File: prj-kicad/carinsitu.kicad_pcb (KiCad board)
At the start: 2 copper layers, 120 x 50 mm, 67 parts, among them P1 BAT, P2 MOT, P3 CONN_3, P4 CONN_4, SW1 SWITCH_SLIDE, SW2 Reset, U1 LoLin_D1_mini_pro, U2 MIC2860, U3 MAX17044G, U4 SN74LV1T34DBV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

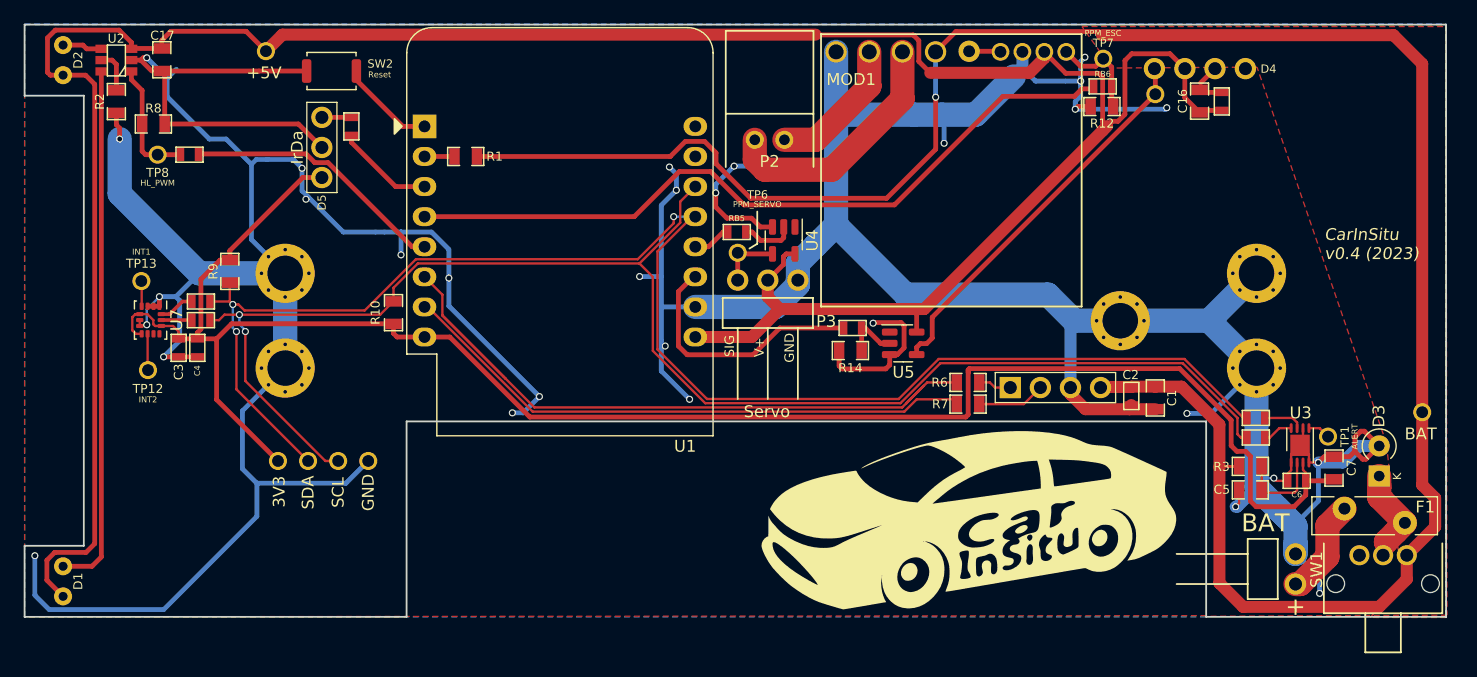
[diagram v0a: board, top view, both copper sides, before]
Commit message: Change some footprints for kicad lib ones + silkscreen + route adjustments
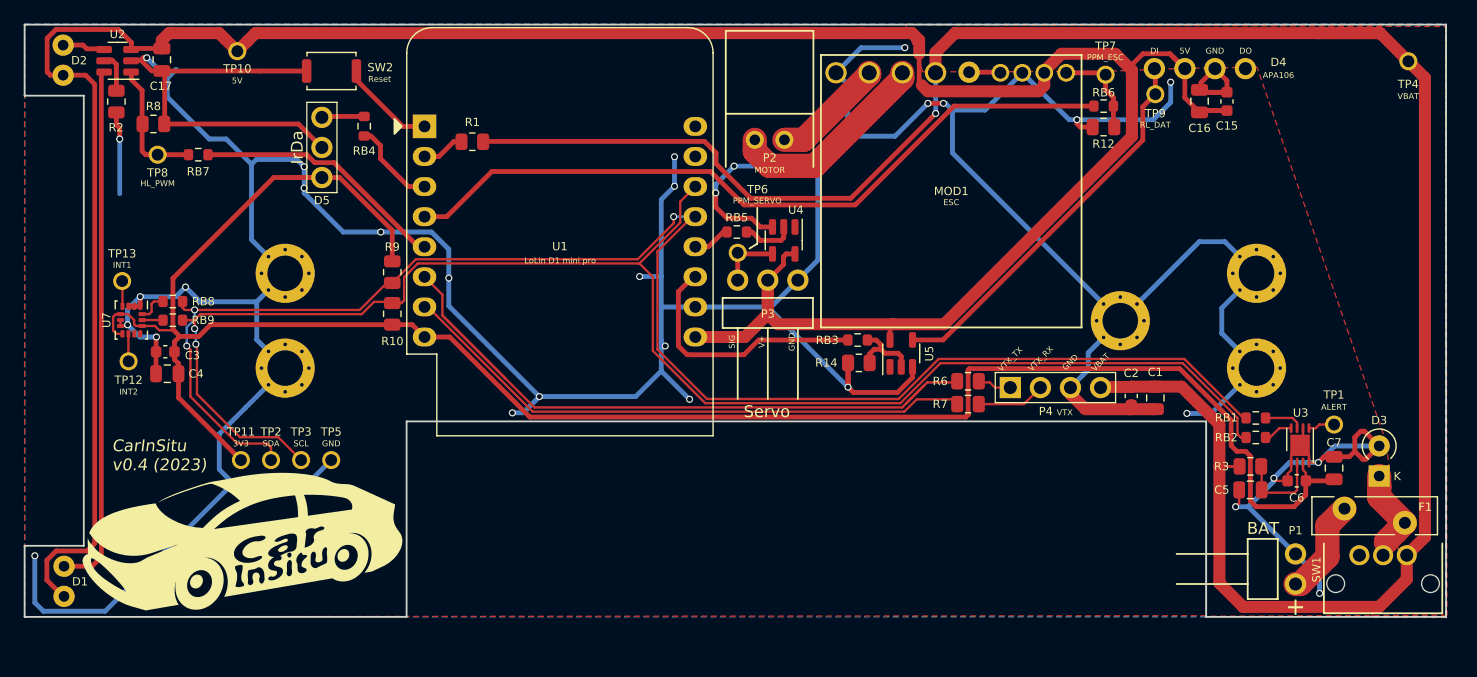
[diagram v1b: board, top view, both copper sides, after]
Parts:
- removed the G*** at (162.5, 121.8)
- added G***: LOGO, logo_carinsitu, F.Cu at (101.1, 123.6)
- C1, C16, C17, C5, C7: footprint carinsitu:SMD0805 -> Capacitor_SMD:C_0805_2012Metric
- C15, C2, C3, C6: footprint carinsitu:SMD0603 -> Capacitor_SMD:C_0603_1608Metric
- C4: footprint carinsitu:SMD0603 -> Capacitor_SMD:C_0805_2012Metric
- D1, D2: footprint carinsitu:LED -> LED_THT:LED_D5.0mm_Horizontal_O3.81mm_Z3.0mm; moved to B.Cu
- R1, R10, R12, R14, R2, R3, R6, R7, R8, R9: footprint carinsitu:SMD0805 -> Resistor_SMD:R_0805_2012Metric
- RB1, RB2, RB3, RB4, RB5, RB6, RB7, RB8, RB9: footprint carinsitu:SMD0603 -> Resistor_SMD:R_0603_1608Metric
- U2: footprint carinsitu:SOT23-6 -> Package_TO_SOT_SMD:SOT-23-6
- moved TP4 29.6 mm to (199.6, 83.1)
- moved R9 13.7 mm to (113.8, 100.9)
- moved C4 3.35 mm to (94.8, 109.5), turned to 0 degrees
- moved TP11 3.13 mm to (101.0, 116.8)
- moved TP2 3.13 mm to (103.6, 116.8)
- moved TP3 3.13 mm to (106.1, 116.8)
- moved TP5 3.13 mm to (108.6, 116.8)
- moved TP10 2.41 mm to (100.7, 82.2)
- moved RB8 2.38 mm to (95.3, 103.4)
- moved RB9 2.38 mm to (95.3, 105.0)
- moved TP12 1.80 mm to (91.5, 108.4)
- moved MOD1 1.77 mm to (161.0, 94.1)
- moved R12 1.74 mm to (173.8, 88.7)
- moved RB6 1.67 mm to (173.8, 86.9)
- moved TP13 1.62 mm to (91.0, 101.7)
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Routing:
- net GND: track 474.7 -> 440.9 mm, vias 30 -> 31
- net +3V3: track 156.9 -> 171.8 mm
- net +5V: track 228.0 -> 238.6 mm
- net Net-(MOD1-Pad3): track 21.0 -> 17.4 mm
- net SCL: track 128.4 -> 131.6 mm
- net Net-(MOD1-Pad2): track 12.0 -> 9.58 mm
- net RL_DAT: track 4.81 -> 6.42 mm
- net SDA: track 129.8 -> 131.3 mm
- net Net-(RB7-Pad1): track 22.3 -> 21.0 mm
- net Net-(R1-Pad1): track 2.52 -> 3.64 mm
- net IR_RX: track 2.49 -> 3.49 mm
- net +VBAT: track 185.2 -> 186.1 mm
- net Net-(RB9-Pad2): track 2.57 -> 1.75 mm
- net Net-(RB4-Pad1): track 8.31 -> 7.51 mm
- net Net-(TP12-Pad1): track 3.03 -> 2.31 mm
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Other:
- board text removed: "+5V"
- board text removed: "3V3"
- board text removed: "BAT"
- board text removed: "GND"
- board text removed: "SCL"
- board text removed: "SDA"

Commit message: Add decoupling capacitors + RB10
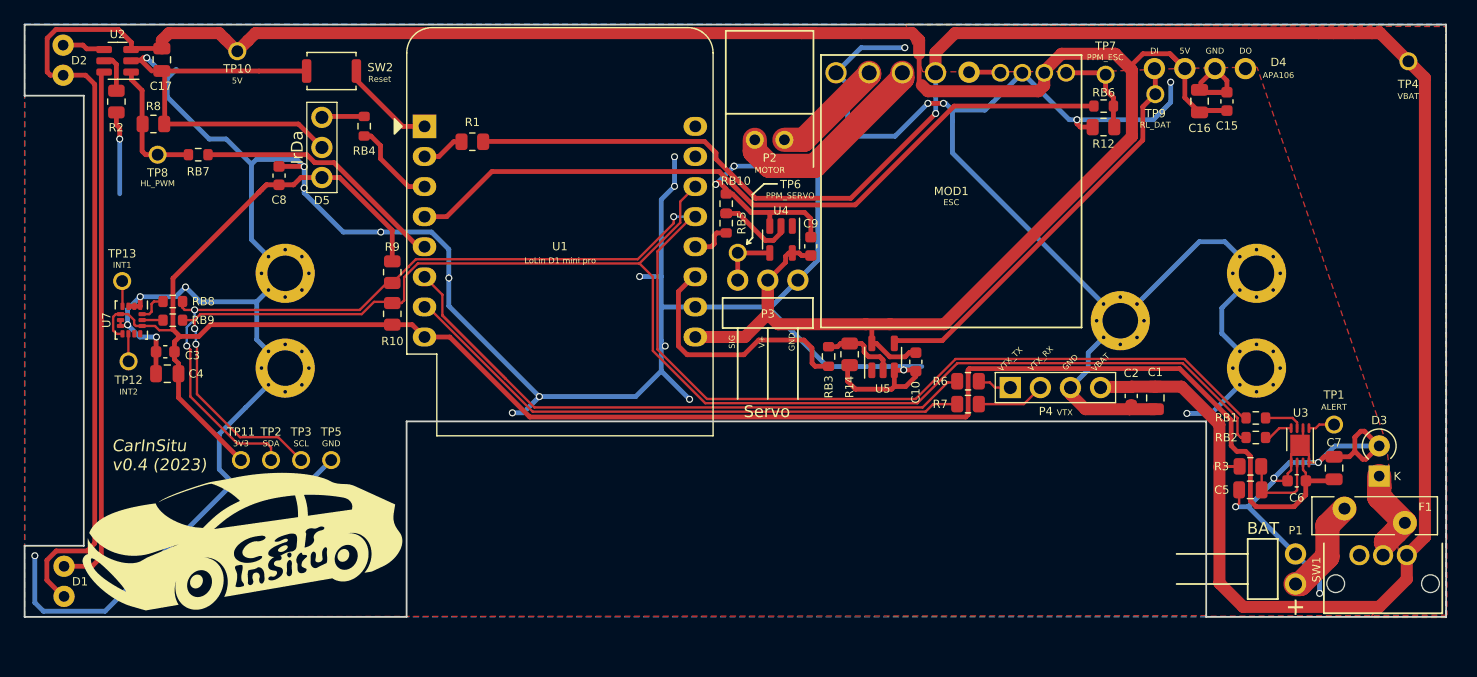
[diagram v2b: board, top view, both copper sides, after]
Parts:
- added C10: 100nF, Capacitor_SMD:C_0603_1608Metric, F.Cu at (158.0, 108.5)
- added C8: 100nF, Capacitor_SMD:C_0603_1608Metric, F.Cu at (104.2, 92.8)
- added C9: 100nF, Capacitor_SMD:C_0603_1608Metric, F.Cu at (149.1, 98.7)
- added RB10: DNP, Resistor_SMD:R_0603_1608Metric, F.Cu at (142.0, 95.1)
- moved RB3 2.82 mm to (150.6, 108.0), turned to 90 degrees
- moved U5 1.56 mm to (155.2, 108.1)
- moved RB5 1.16 mm to (142.0, 96.8), turned to 90 degrees
- moved R14 1.06 mm to (152.4, 107.8), turned to 90 degrees
- moved U4 0.24 mm to (146.6, 98.1)
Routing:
- net GND: track 440.9 -> 453.9 mm
- net +5V: track 238.6 -> 244.5 mm
- net /LOLIN_RX_SWAP: track 61.1 -> 58.9 mm
- net PPM_SERVO: track 4.50 -> 6.41 mm
- net Net-(D4-Pad4): track 32.8 -> 34.5 mm
- net +3V3: track 171.8 -> 170.4 mm

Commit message: Move U3 and its companions
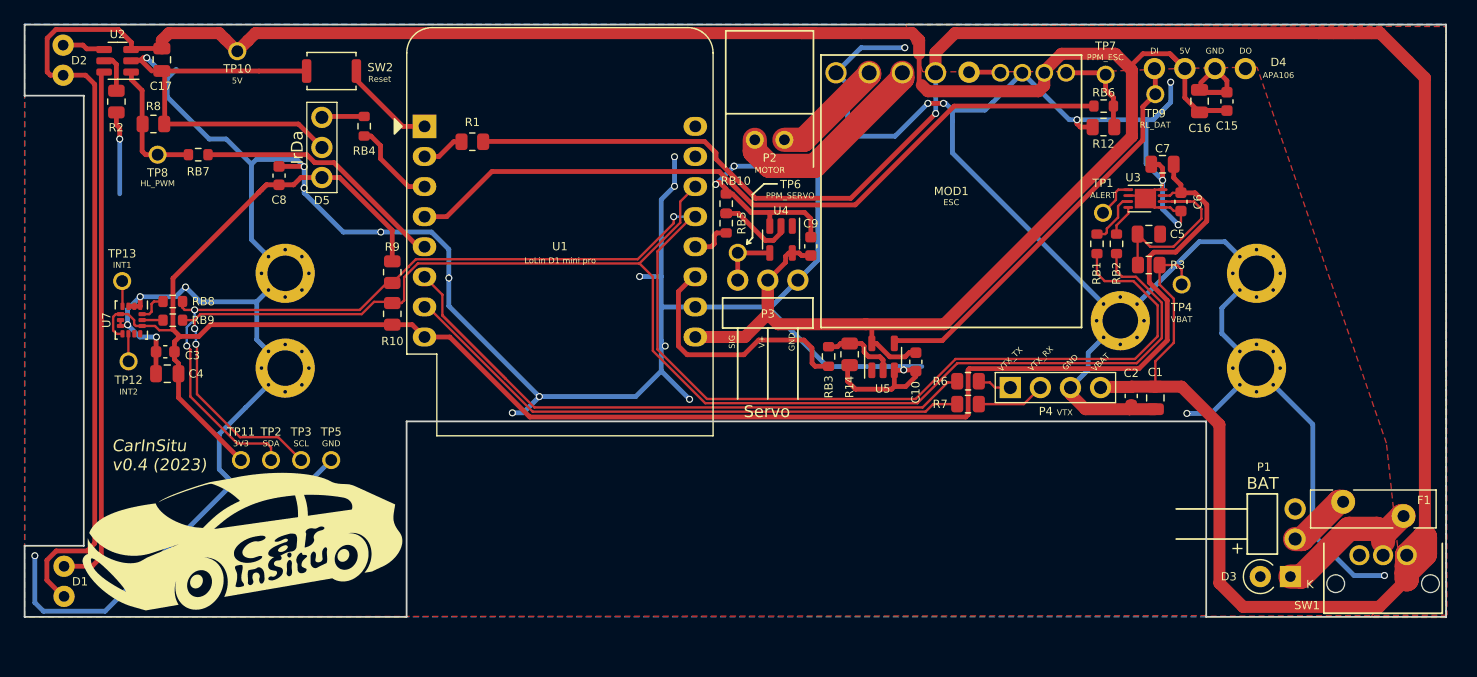
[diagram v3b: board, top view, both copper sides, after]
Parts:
- moved C7 29.5 mm to (178.8, 91.8), turned to 180 degrees
- moved TP4 26.9 mm to (180.4, 101.9)
- moved TP1 26.5 mm to (173.8, 95.9)
- moved C6 25.5 mm to (180.4, 95.0), turned to -90 degrees
- moved U3 24.6 mm to (177.4, 94.7), turned to 180 degrees
- moved C5 23.2 mm to (177.7, 97.7), turned to 0 degrees
- moved RB2 20.1 mm to (174.9, 98.5), turned to -90 degrees
- moved RB1 19.9 mm to (173.3, 98.5), turned to -90 degrees
- moved R3 19.0 mm to (177.7, 100.3), turned to 180 degrees
- moved D3 11.3 mm to (189.6, 126.6), turned to 180 degrees
- moved P1 3.80 mm to (190.0, 122.2)
- moved F1 0.58 mm to (199.2, 121.5)
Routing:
- net +VBAT: track 185.8 -> 205.3 mm
- net Net-(C5-Pad1): track 7.15 -> 15.3 mm
- net Net-(D3-Pad1): track 9.56 -> 13.8 mm
- net Net-(F1-Pad2): track 8.31 -> 5.35 mm
- net +3V3: track 170.4 -> 167.9 mm
- net GND: track 453.9 -> 451.5 mm, vias 31 -> 30
- net SDA: track 131.3 -> 133.3 mm
- net Net-(RB1-Pad1): track 3.36 -> 4.53 mm
- net Net-(TP1-Pad1): track 2.25 -> 3.33 mm
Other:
- board text removed: "+"

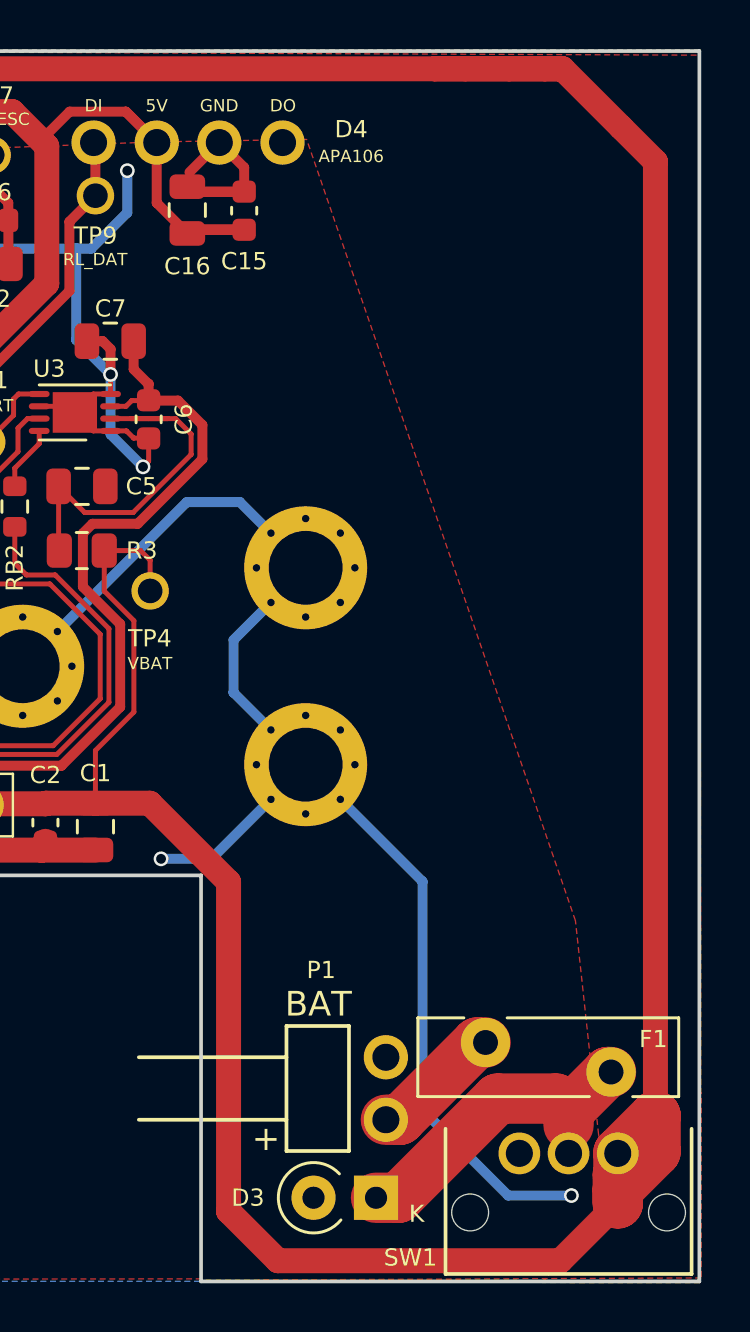
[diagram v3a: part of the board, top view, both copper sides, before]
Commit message: Add VTX holes (WIP, bottom right needs rerouting)
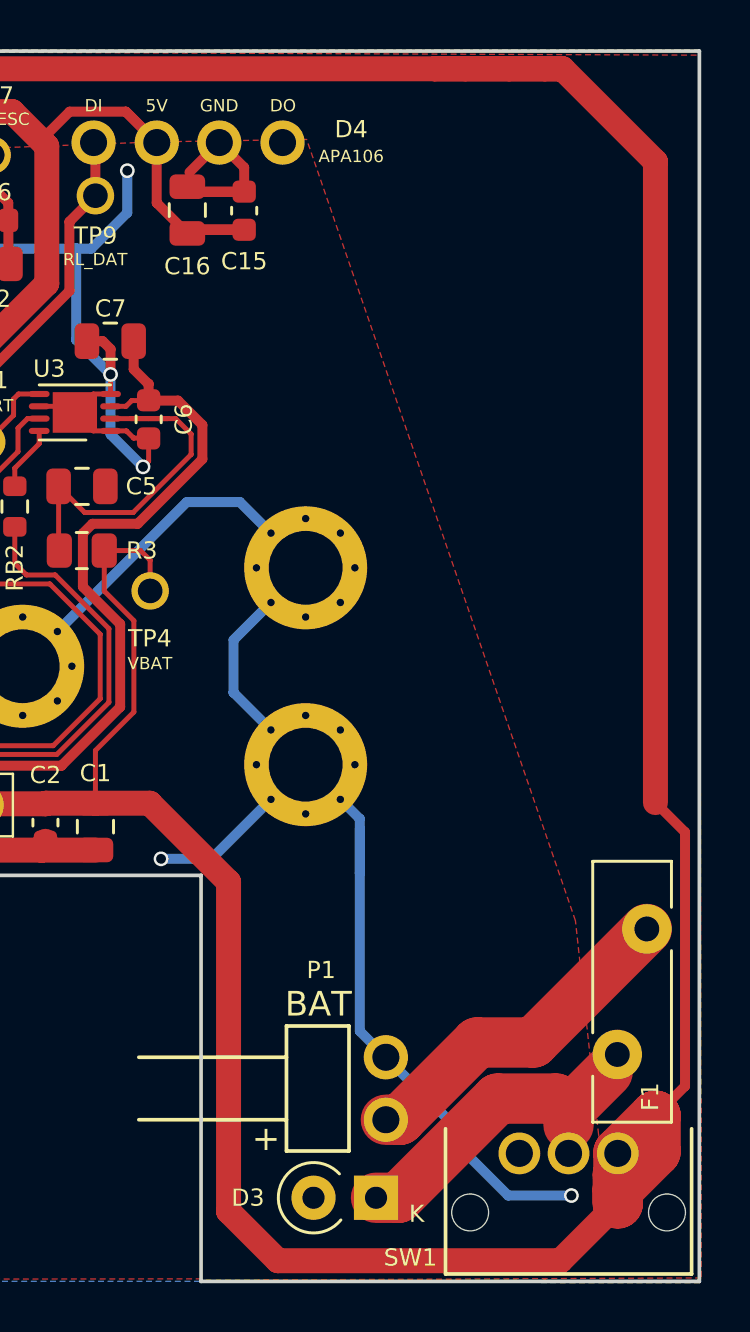
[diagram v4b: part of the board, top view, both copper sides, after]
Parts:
- added H1: VTX_avatar_halfholes, carinsitu:VTX_avatar_halfholes, F.Cu at (181.0, 105.0)
- moved F1 0.76 mm to (199.4, 120.8), turned to 90 degrees
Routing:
- net Net-(F1-Pad2): track 5.35 -> 13.8 mm
- net GND: track 451.5 -> 453.4 mm

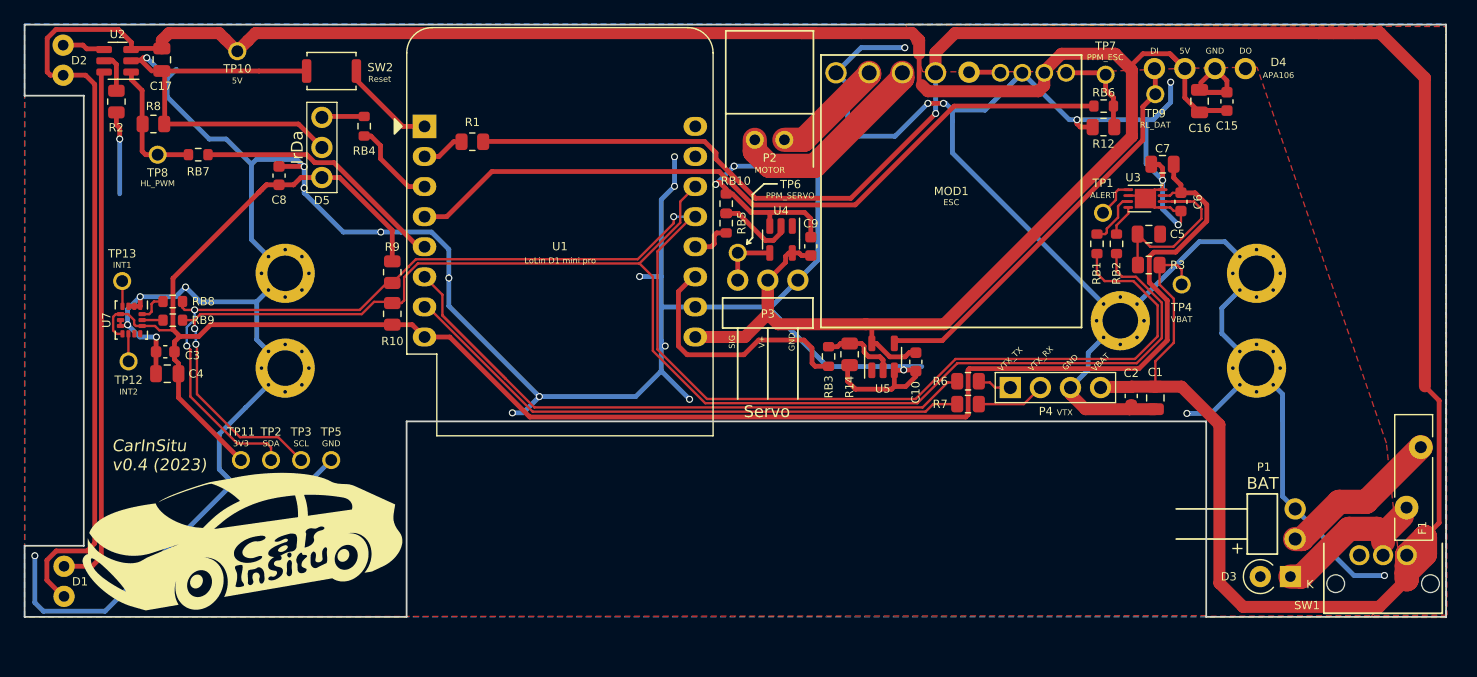
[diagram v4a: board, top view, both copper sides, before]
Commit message: Change input protection and its routing
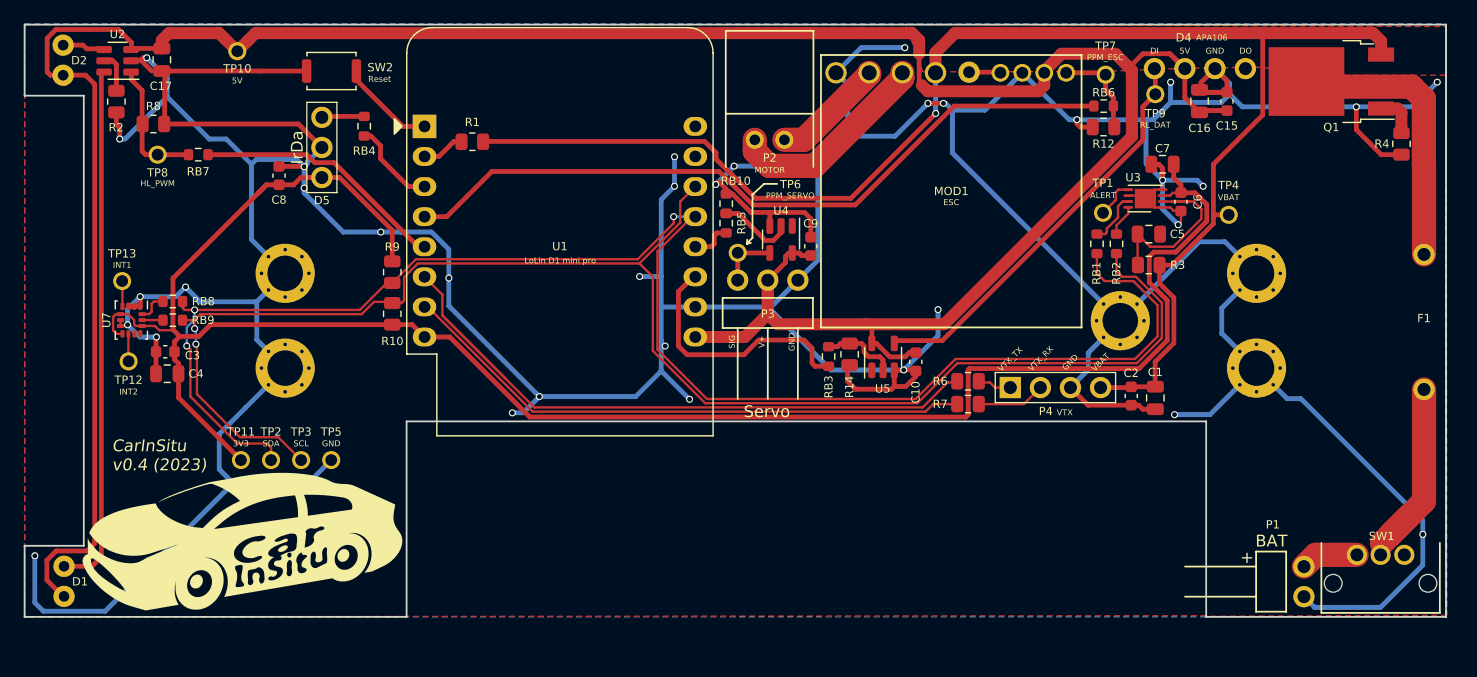
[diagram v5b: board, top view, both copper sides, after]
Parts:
- removed D3: D, Diode_THT:D_A-405_P2.54mm_Vertical_KathodeUp
- added Q1: TJ15P04M3, Package_TO_SOT_SMD:TO-252-2, F.Cu at (193.1, 84.8)
- added R4: 1k, Resistor_SMD:R_0805_2012Metric, F.Cu at (199.0, 90.1)
- F1: value Polyfuse -> Fuse_Small; footprint Fuse:Fuse_Bourns_MF-RG500 -> Fuse:Fuse_Littelfuse-LVR100
- H1: value VTX_avatar_halfholes -> MountingHole
- moved F1 10.1 mm to (200.9, 110.8)
- moved TP4 7.09 mm to (184.4, 96.1)
- moved P1 4.92 mm to (190.8, 127.0)
- moved SW1 0.21 mm to (195.2, 124.8)
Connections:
- P1 pad 1: GND -> Net-(P1-Pad1)
- P1 pad 2: Net-(F1-Pad2) -> GND
- SW1 pad 1: unconnected-(SW1-Pad1) -> Net-(P1-Pad1)
- SW1 pad 3: +VBAT -> unconnected-(SW1-Pad3)
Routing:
- net +VBAT: track 205.3 -> 133.9 mm
- net GND: track 453.4 -> 507.3 mm, vias 30 -> 34
- net Net-(F1-Pad2): track 13.8 -> 23.7 mm
- net Net-(P1-Pad1): track 0.00 -> 4.85 mm
- net Net-(F1-Pad1): track 13.7 -> 17.7 mm
- net Net-(Q1-Pad1): track 0.00 -> 3.60 mm

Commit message: Adjust small things on PCB
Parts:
- moved P1 0.23 mm to (190.8, 126.8)
- moved R2 0.10 mm to (90.6, 86.5)
- moved R8 0.05 mm to (93.7, 88.4)
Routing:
- net +5V: track 244.5 -> 243.4 mm
- net Net-(D1-Pad2): track 44.5 -> 43.9 mm
- net Net-(F1-Pad2): track 23.7 -> 23.0 mm
